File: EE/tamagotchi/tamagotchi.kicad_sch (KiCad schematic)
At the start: 0 parts

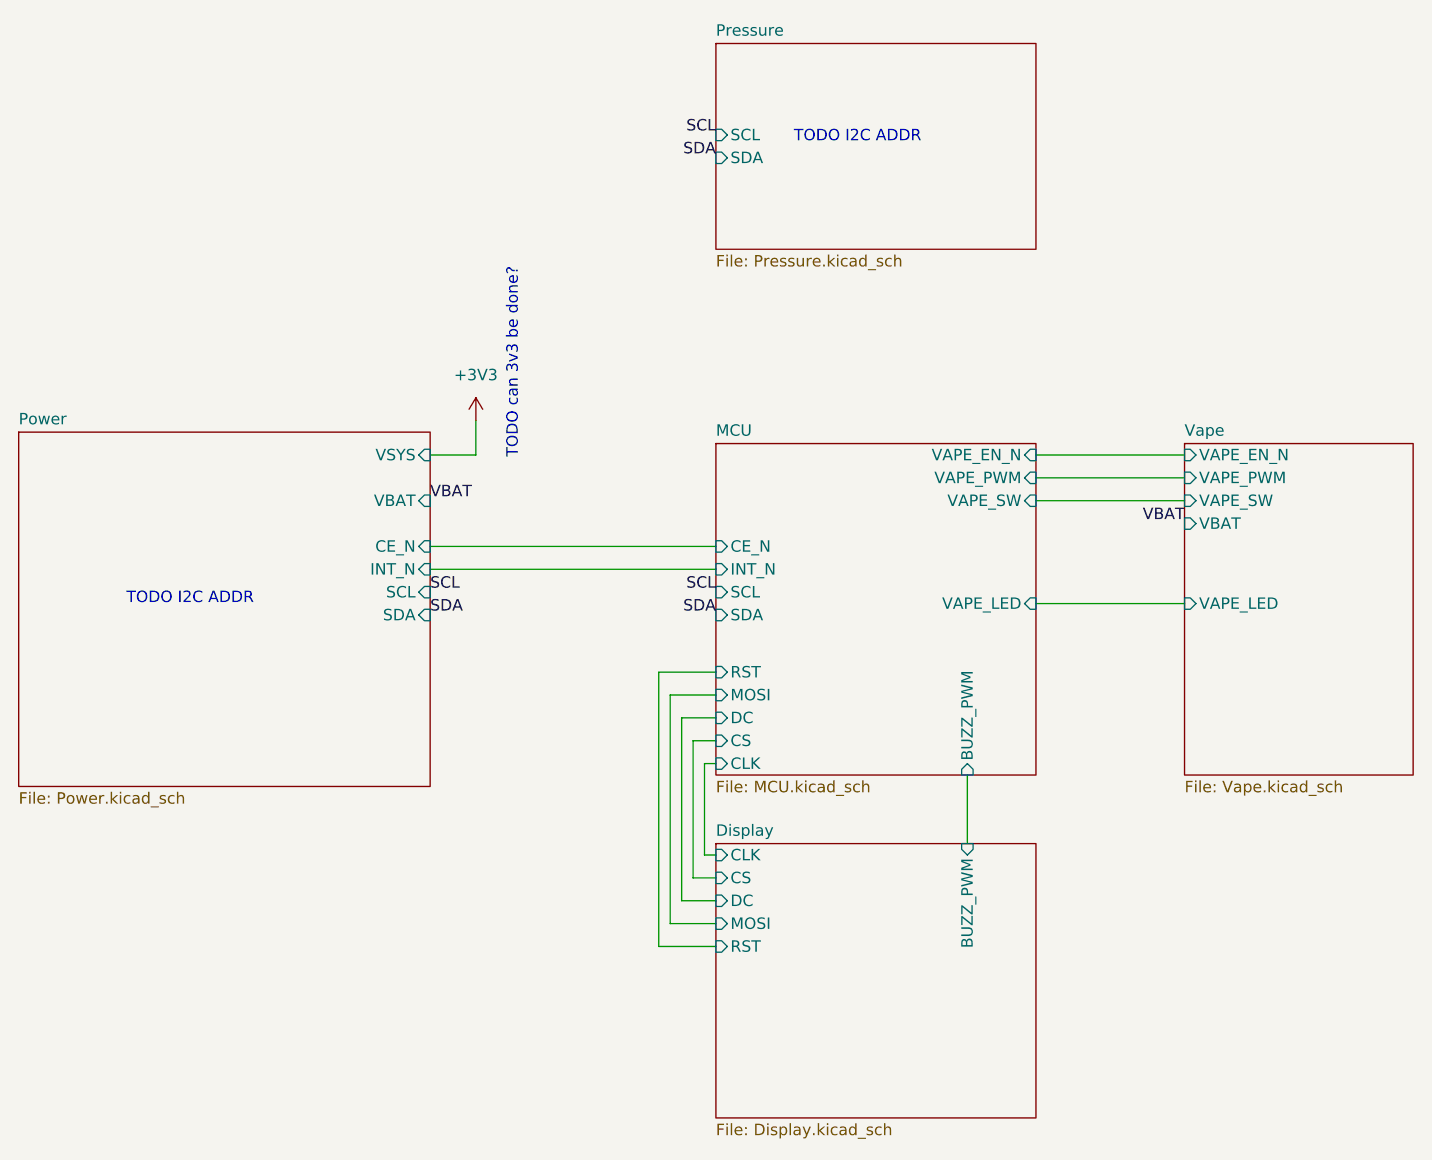
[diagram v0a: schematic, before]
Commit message: WIP - Overall Cleanup, Power Change
Added expected loads for power in schematic.
Changed power arch to use existing design that appears to work.
Removed rear backlight LEDs - shouldn't be necessary.
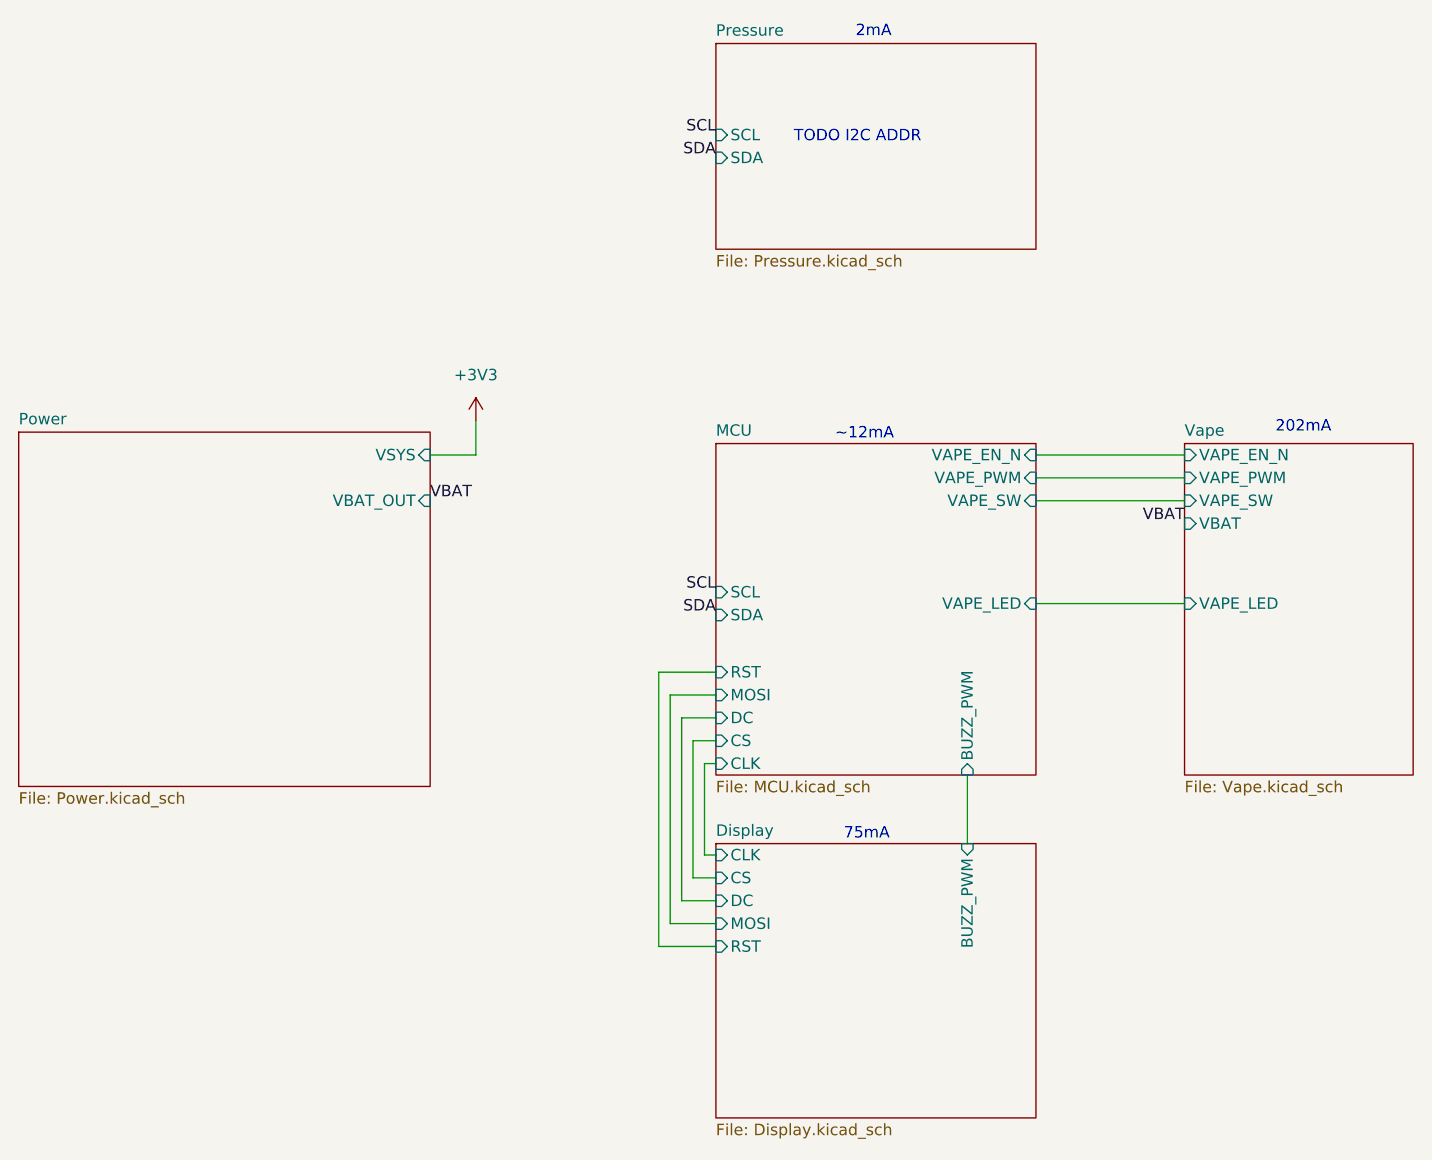
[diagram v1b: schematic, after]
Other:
- sheet MCU ports: added none; removed CE_N, INT_N
- sheet Power ports: added VBAT_OUT; removed CE_N, INT_N, SCL, SDA, VBAT
- note added: "202mA"
- note added: "2mA"
- note added: "75mA"
- note added: "~12mA"
- note removed: "TODO can 3v3 be done?"
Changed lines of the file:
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@@
 	(generator_version "9.0")
 	(paper "A4")
+	(text "~12mA"
+		(exclude_from_sim no)
+		(at 146.05 89.154 0)
+		(effects
+			(font
+				(size 1.27 1.27)
+			)
+		)
+	)
 	(text "TODO I2C ADDR"
 		(exclude_from_sim no)
@@
 		)
 	)
-	(text "TODO can 3v3 be done?"
-		(exclude_from_sim no)
-		(at 106.934 81.28 90)
-		(effects
-			(font
-				(size 1.27 1.27)
-			)
-		)
-	)
-	(text "TODO I2C ADDR"
-		(exclude_from_sim no)
-		(at 71.12 107.442 0)
+	(text "202mA"
+		(exclude_from_sim no)
+		(at 194.818 88.392 0)
+		(effects
+			(font
+				(size 1.27 1.27)
+			)
+		)
+	)
+	(text "2mA"
+		(exclude_from_sim no)
+		(at 147.066 44.45 0)
+		(effects
+			(font
+				(size 1.27 1.27)
+			)
+		)
+	)
+	(text "75mA"
+		(exclude_from_sim no)
+		(at 146.304 133.604 0)
 		(effects
 			(font
@@
 	(wire
 		(pts
-			(xy 97.79 101.6) (xy 129.54 101.6)
-		)
-		(stroke
-			(width 0)
-			(type default)
-		)
-	)
-	(wire
-		(pts
 			(xy 124.46 118.11) (xy 129.54 118.11)
 		)
@@
 	(wire
 		(pts
-			(xy 97.79 104.14) (xy 129.54 104.14)
-		)
-		(stroke
-			(width 0)
-			(type default)
-		)
-	)
-	(wire
-		(pts
 			(xy 127 138.43) (xy 129.54 138.43)
 		)
@@
 			(width 0)
 			(type default)
-		)
-	)
-	(label "SCL"
-		(at 97.79 106.68 0)
-		(effects
-			(font
-				(size 1.27 1.27)
-			)
-			(justify left bottom)
 		)
 	)
 	(label "VBAT"
 		(at 97.79 96.52 0)
-		(effects
-			(font
-				(size 1.27 1.27)
-			)
-			(justify left bottom)
-		)
-	)
-	(label "SDA"
-		(at 97.79 109.22 0)
 		(effects
 			(font
@@
 			)
 		)
-		(pin "CE_N" input
-			(at 97.79 101.6 0)
-			(effects
-				(font
-					(size 1.27 1.27)
-				)
-				(justify right)
-			)
-		)
-		(pin "INT_N" input
-			(at 97.79 104.14 0)
-			(effects
-				(font
-					(size 1.27 1.27)
-				)
-				(justify right)
-			)
-		)
-		(pin "SCL" input
-			(at 97.79 106.68 0)
-			(effects
-				(font
-					(size 1.27 1.27)
-				)
-				(justify right)
-			)
-		)
-		(pin "SDA" input
-			(at 97.79 109.22 0)
-			(effects
-				(font
-					(size 1.27 1.27)
-				)
-				(justify right)
-			)
-		)
 		(pin "VSYS" input
 			(at 97.79 91.44 0)
@@
 			)
 		)
-		(pin "VBAT" input
+		(pin "VBAT_OUT" input
 			(at 97.79 96.52 0)
 			(effects
@@
 			)
 		)
-		(pin "CE_N" input
-			(at 129.54 101.6 180)
-			(effects
-				(font
-					(size 1.27 1.27)
-				)
-				(justify left)
-			)
-		)
-		(pin "INT_N" input
-			(at 129.54 104.14 180)
-			(effects
-				(font
-					(size 1.27 1.27)
-				)
-				(justify left)
-			)
-		)
